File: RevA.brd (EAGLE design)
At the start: 106 x 53 mm, 61 parts, among them IC1 MAX31855, IC10 DS3231/SO, IC3 MAX31855, IC4 MAX31855, IC5 MAX31855, IC9 ATMEGA32U4-AU, J1 1X2-3.5MM, J2 1X2-3.5MM, J3 1X2-3.5MM, J4 1X2-3.5MM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

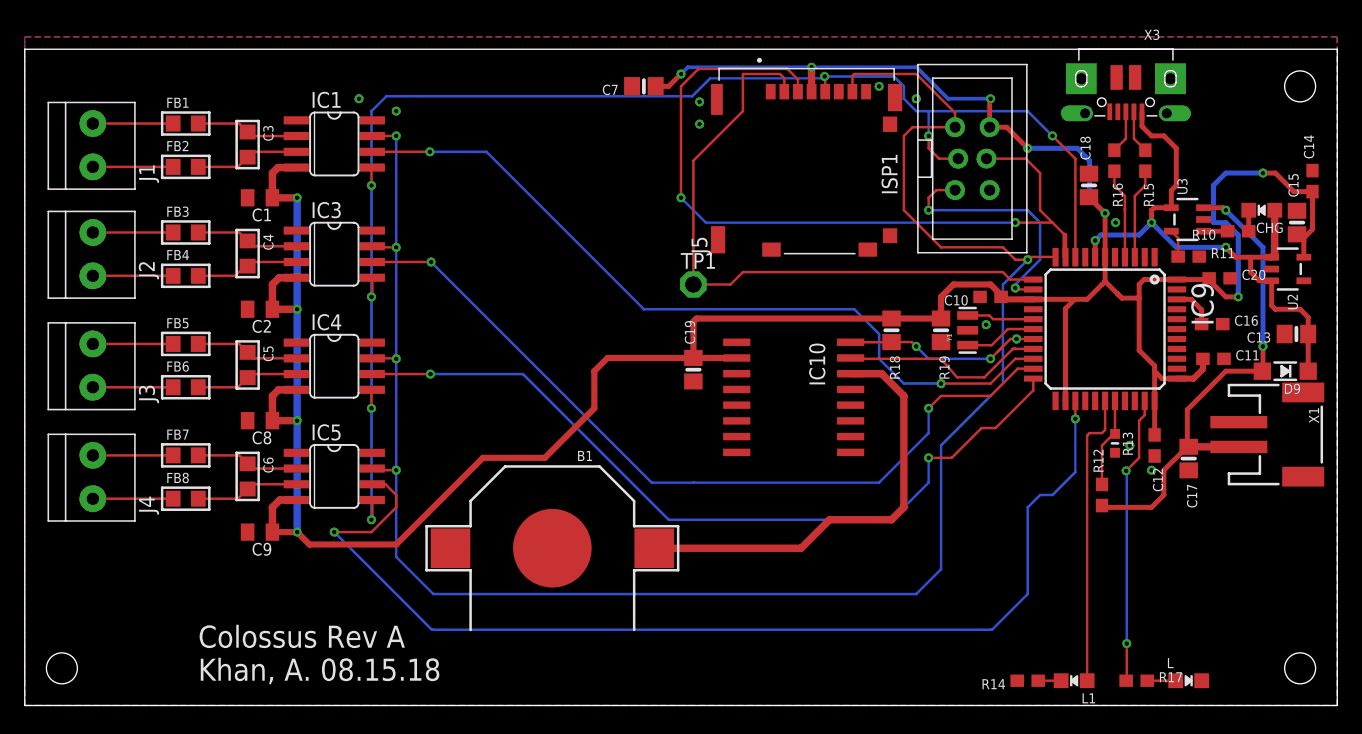
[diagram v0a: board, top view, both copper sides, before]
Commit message: Reduced Footprint
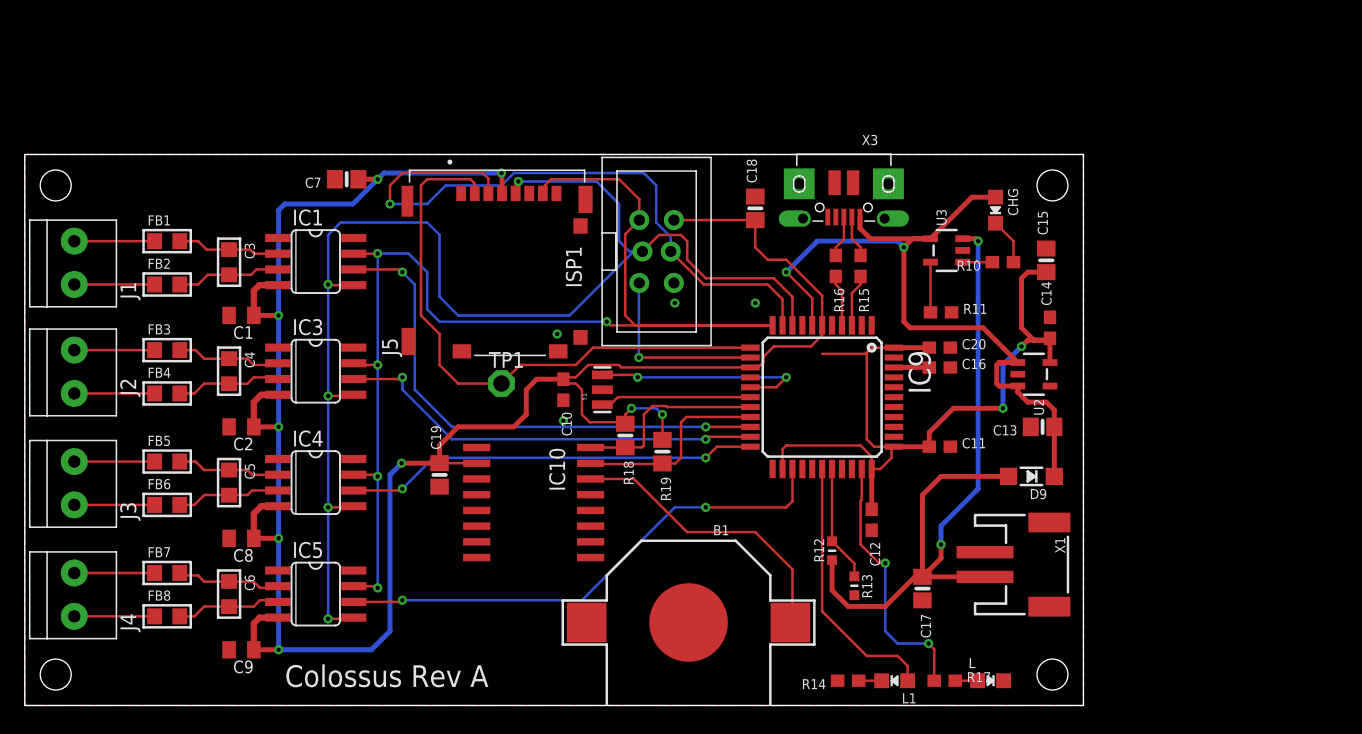
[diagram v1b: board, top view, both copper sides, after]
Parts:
- R12: device microbuilder:0603-NO -> microbuilder:_0603MP
- moved C10 35.3 mm to (43.5, 25.5), turned to 270 degrees
- moved Y1 29.9 mm to (46.6, 25.5)
- moved C18 27.0 mm to (59.0, 40.1)
- moved ISP1 26.6 mm to (51.0, 36.7)
- moved J5 26.3 mm to (38.1, 35.0)
- moved C7 25.1 mm to (26.0, 42.5)
- moved R19 24.5 mm to (51.5, 20.5)
- moved R15 24.5 mm to (67.5, 35.5)
- moved X3 24.3 mm to (66.2, 40.2)
- moved C14 24.3 mm to (82.8, 30.5)
- moved R16 24.1 mm to (65.5, 35.5)
- moved R13 24.0 mm to (67.0, 9.67)
- moved C17 23.9 mm to (72.5, 9.44)
- moved C12 23.6 mm to (68.4, 15.0)
- moved IC9 23.5 mm to (64.4, 24.9)
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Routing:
- net MISO: track 153.0 -> 102.2 mm
- net CS-4: track 87.8 -> 41.4 mm
- net CS-3: track 64.7 -> 33.5 mm
- net CS-2: track 65.7 -> 34.8 mm
- net CS-1: track 63.1 -> 42.3 mm
- net VBAT: track 40.9 -> 60.8 mm
- net VBUS: track 46.5 -> 62.8 mm, vias 3 -> 2
- net N$29: track 6.07 -> 18.7 mm, vias 0 -> 2
- net VCR: track 35.6 -> 23.7 mm
- net MOSI: track 63.7 -> 52.7 mm, vias 2 -> 1
- net SCK: track 115.5 -> 106.8 mm, vias 7 -> 5
- net N$30: track 5.84 -> 12.3 mm
- net +3V3: track 254.7 -> 248.5 mm
- net RST: track 20.4 -> 15.2 mm, vias 2 -> 1
- net SD_CS: track 51.3 -> 47.5 mm
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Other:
- board size 106 x 53 mm -> 85.5 x 44.5 mm
- board text added: "Colossus Rev A"
- board text removed: "Colossus Rev A Khan, A. 08.15.18"

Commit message: Added BOM
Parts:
- added C21: 10µF, microbuilder:0805-NO
- moved C16 2.87 mm to (72.2, 24.9), turned to 270 degrees
- moved D9 1.92 mm to (82.8, 19.7), turned to 270 degrees
- moved R11 1.72 mm to (73.2, 33.2), turned to 270 degrees
- moved C11 1.58 mm to (72.4, 20.4), turned to 270 degrees
- moved C13 1.50 mm to (80.7, 22.5), turned to 90 degrees
- moved C20 0.85 mm to (73.9, 28.1), turned to 270 degrees
- moved R10 0.71 mm to (78.5, 36.3), turned to 270 degrees
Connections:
- net GND: now also C21.1
- net VBUS: now also C21.2
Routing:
- net +3V3: track 248.5 -> 252.1 mm
- net VBUS: track 62.8 -> 66.2 mm
- net VBAT: track 60.8 -> 64.0 mm
- net N$27: track 4.05 -> 1.70 mm
- net N$25: track 3.75 -> 1.84 mm
- net SCK: track 106.8 -> 105.2 mm, vias 5 -> 6

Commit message: Final Traces
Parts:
- moved C11 12.8 mm to (60.0, 17.1), turned to 180 degrees
- moved D9 2.55 mm to (80.3, 19.2)
- moved C13 1.13 mm to (81.5, 23.3), turned to 0 degrees
- moved Y1 0.50 mm to (47.1, 25.5)
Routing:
- net MISO: track 102.2 -> 90.9 mm
- net VBAT: track 64.0 -> 54.7 mm
- net N$29: track 18.7 -> 11.9 mm, vias 2 -> 0
- net VBUS: track 66.2 -> 59.4 mm
- net RST: track 15.2 -> 11.5 mm
- net N$30: track 12.3 -> 11.7 mm
- net GND: track 0.00 -> 0.62 mm, vias 8 -> 28

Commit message: Cleaned up the layout
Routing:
- net GND: vias 28 -> 48
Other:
- board text added: "+"

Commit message: Final cleanup
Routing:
- net GND: vias 48 -> 59
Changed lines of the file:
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@@
 <drawing>
 <settings>
-<setting alwaysvectorfont="yes"/>
+<setting alwaysvectorfont="no"/>
 <setting verticaltext="up"/>
 </settings>
@@
 </layers>
 <board>
-<fusionsync huburn="a.cGVyc29uYWw6dWUyYmRkYjQx" projecturn="a.cGVyc29uYWw6dWUyYmRkYjQxIzIwMTgwNTAyMTMwMjU4MzAx" f3durn="urn:adsk.wipprod:dm.lineage:a68wfmUxQy2LyGLi9FcYGg" pcbguid="62a8e096-691a-4df0-bd8f-1dbb8bf064d3" lastpulledtime="" lastsyncedchangeguid="620a17bd-b7ee-07cf-b851-2800ced5cc59"/>
+<fusionsync huburn="a.cGVyc29uYWw6dWUyYmRkYjQx" projecturn="a.cGVyc29uYWw6dWUyYmRkYjQxIzIwMTgwNTAyMTMwMjU4MzAx" f3durn="urn:adsk.wipprod:dm.lineage:a68wfmUxQy2LyGLi9FcYGg" pcbguid="62a8e096-691a-4df0-bd8f-1dbb8bf064d3" lastpulledtime="" lastsyncedchangeguid="5deacc8e-e9a5-6dbb-9bdc-3b0ce5d54393"/>
 <plain>
 <wire x1="0" y1="0" x2="85.5" y2="0" width="0" layer="20"/>
@@
 <hole x="2.5" y="42" drill="2.5"/>
 <text x="24.5" y="1.5" size="1.778" layer="29" font="vector" ratio="12">Colossus Rev A</text>
-<text x="73.875" y="8.375" size="2" layer="25">+</text>
+<text x="73.875" y="8.25" size="2" layer="25">+</text>
 </plain>
 <attributes>
@@
 <via x="49" y="17.5" extent="1-16" drill="0.35"/>
 <via x="53.25" y="19.25" extent="1-16" drill="0.35"/>
+<via x="44.5" y="28.5" extent="1-16" drill="0.35"/>
+<via x="78.125" y="23" extent="1-16" drill="0.35"/>
+<via x="76.125" y="18" extent="1-16" drill="0.35"/>
+<via x="70.25" y="3.25" extent="1-16" drill="0.35"/>
+<via x="68.75" y="6.25" extent="1-16" drill="0.35"/>
+<via x="30.25" y="24.75" extent="1-16" drill="0.35"/>
+<via x="29.25" y="19.75" extent="1-16" drill="0.35"/>
+<via x="31" y="16.625" extent="1-16" drill="0.35"/>
+<via x="78.5" y="18.25" extent="1-16" drill="0.35"/>
+<via x="63.75" y="38.25" extent="1-16" drill="0.35"/>
+<via x="70.625" y="11.25" extent="1-16" drill="0.35"/>
 </signal>
 <signal name="CS-1">

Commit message: Adding gerber files
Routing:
- net GND: vias 59 -> 71
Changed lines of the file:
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@@
 <layer number="26" name="bNames" color="7" fill="1" visible="no" active="yes"/>
 <layer number="27" name="tValues" color="7" fill="1" visible="yes" active="yes"/>
-<layer number="28" name="bValues" color="7" fill="1" visible="no" active="yes"/>
+<layer number="28" name="bValues" color="7" fill="1" visible="yes" active="yes"/>
 <layer number="29" name="tStop" color="7" fill="3" visible="yes" active="yes"/>
 <layer number="30" name="bStop" color="7" fill="6" visible="yes" active="yes"/>
@@
 </layers>
 <board>
-<fusionsync huburn="a.cGVyc29uYWw6dWUyYmRkYjQx" projecturn="a.cGVyc29uYWw6dWUyYmRkYjQxIzIwMTgwNTAyMTMwMjU4MzAx" f3durn="urn:adsk.wipprod:dm.lineage:a68wfmUxQy2LyGLi9FcYGg" pcbguid="62a8e096-691a-4df0-bd8f-1dbb8bf064d3" lastpulledtime="" lastsyncedchangeguid="5deacc8e-e9a5-6dbb-9bdc-3b0ce5d54393"/>
+<fusionsync huburn="a.cGVyc29uYWw6dWUyYmRkYjQx" projecturn="a.cGVyc29uYWw6dWUyYmRkYjQxIzIwMTgwNTAyMTMwMjU4MzAx" f3durn="urn:adsk.wipprod:dm.lineage:a68wfmUxQy2LyGLi9FcYGg" pcbguid="62a8e096-691a-4df0-bd8f-1dbb8bf064d3" lastpulledtime="" lastsyncedchangeguid="a59ad179-57a4-5a50-164f-14a713c3d576"/>
 <plain>
 <wire x1="0" y1="0" x2="85.5" y2="0" width="0" layer="20"/>
@@
 </element>
 <element name="C10" library="microbuilder" package="0603-NO" value="1uF" x="43.5" y="25.5" smashed="yes" rot="R270">
-<attribute name="NAME" x="42.748" y="22.972" size="0.8128" layer="25" font="vector" ratio="10"/>
+<attribute name="NAME" x="42.248" y="23.097" size="0.8128" layer="25" font="vector" ratio="10"/>
 </element>
 <element name="C11" library="microbuilder" package="0603-NO" value="1uF" x="60.025" y="17.15" smashed="yes" rot="R180">
@@
 <contactref element="C20" pad="2"/>
 <via x="43" y="30" extent="1-16" drill="0.35"/>
-<via x="45.75" y="23.75" extent="1-16" drill="0.35"/>
+<via x="44.5" y="22.875" extent="1-16" drill="0.35"/>
 <via x="52.5" y="32.5" extent="1-16" drill="0.35"/>
 <via x="59" y="32.5" extent="1-16" drill="0.35"/>
@@
 <via x="63.75" y="38.25" extent="1-16" drill="0.35"/>
 <via x="70.625" y="11.25" extent="1-16" drill="0.35"/>
+<via x="33.375" y="32.125" extent="1-16" drill="0.35"/>
+<via x="32.75" y="29.75" extent="1-16" drill="0.35"/>
+<via x="35.25" y="26.75" extent="1-16" drill="0.35"/>
+<via x="40.25" y="26.75" extent="1-16" drill="0.35"/>
+<via x="39.25" y="23.75" extent="1-16" drill="0.35"/>
+<via x="30.75" y="33.75" extent="1-16" drill="0.35"/>
+<via x="67.25" y="3.75" extent="1-16" drill="0.35"/>
+<via x="49.5" y="42.125" extent="1-16" drill="0.35"/>
+<via x="79.375" y="24.875" extent="1-16" drill="0.35"/>
+<via x="73.25" y="14.875" extent="1-16" drill="0.35"/>
+<via x="70" y="36.625" extent="1-16" drill="0.35"/>
+<via x="45.25" y="9.75" extent="1-16" drill="0.35"/>
 </signal>
 <signal name="CS-1">
@@
 <wire x1="46.375" y1="28.375" x2="54.625" y2="28.375" width="0.4" layer="1"/>
 <wire x1="33.5" y1="19.57" x2="33.505" y2="19.565" width="0.2032" layer="1"/>
-<wire x1="33.505" y1="19.565" x2="36.5" y2="19.565" width="0.2032" layer="1"/>
+<wire x1="33.505" y1="19.565" x2="36.5" y2="19.565" width="0.4" layer="1"/>
 <wire x1="68.4" y1="19.1" x2="68.4" y2="16" width="0.4" layer="1"/>
 <wire x1="68.4" y1="16" x2="68.4" y2="15.85" width="0.4" layer="1"/>
@@
 <wire x1="81" y1="35" x2="80.5" y2="34.5" width="0.4" layer="1"/>
 <wire x1="48.5" y1="22.75" x2="48.625" y2="22.875" width="0.2032" layer="1"/>
-<wire x1="45.625" y1="22.875" x2="45" y2="23.5" width="0.2032" layer="1"/>
-<wire x1="45.625" y1="22.875" x2="48.625" y2="22.875" width="0.2032" layer="1"/>
+<wire x1="45.625" y1="22.875" x2="45" y2="23.5" width="0.4" layer="1"/>
+<wire x1="45.625" y1="22.875" x2="48.625" y2="22.875" width="0.4" layer="1"/>
 <wire x1="20.5" y1="4.5" x2="28" y2="4.5" width="0.4" layer="16"/>
 <wire x1="30.43" y1="19.57" x2="33.5" y2="19.57" width="0.4" layer="1"/>
@@
 <wire x1="78.5" y1="27.5" x2="80.5" y2="29.5" width="0.4" layer="16"/>
 <via x="80.5" y="29.5" extent="1-16" drill="0.35"/>
-<wire x1="48.5" y1="22.75" x2="48.5" y2="23.5" width="0.2032" layer="1"/>
-<wire x1="48.5" y1="23.5" x2="49" y2="24" width="0.2032" layer="1"/>
+<wire x1="48.5" y1="22.75" x2="48.5" y2="23.5" width="0.4" layer="1"/>
+<wire x1="48.5" y1="23.5" x2="49" y2="24" width="0.4" layer="1"/>
 <via x="49" y="24" extent="1-16" drill="0.35"/>
-<wire x1="49" y1="24" x2="50.875" y2="24" width="0.2032" layer="16"/>
-<wire x1="50.875" y1="24" x2="51.5" y2="23.375" width="0.2032" layer="16"/>
+<wire x1="49" y1="24" x2="50.875" y2="24" width="0.4" layer="16"/>
+<wire x1="50.875" y1="24" x2="51.5" y2="23.375" width="0.4" layer="16"/>
 <via x="51.5" y="23.375" extent="1-16" drill="0.35"/>
-<wire x1="51.5" y1="23.375" x2="51.5" y2="21.45" width="0.2032" layer="1"/>
+<wire x1="51.5" y1="23.375" x2="51.5" y2="21.45" width="0.4" layer="1"/>
 <via x="30.43" y="19.57" extent="1-16" drill="0.35"/>
 <wire x1="70.2" y1="28.9" x2="73.9" y2="28.9" width="0.4" layer="1"/>
@@
 <wire x1="68.4" y1="19.1" x2="68.5" y2="19.1" width="0.2032" layer="1"/>
 <wire x1="68.5" y1="19.1" x2="68.5" y2="20.9" width="0.4" layer="1"/>
-<wire x1="61.2" y1="19.1" x2="61.2" y2="17.475" width="0.2032" layer="1"/>
+<wire x1="61.2" y1="19.1" x2="61.2" y2="17.475" width="0.4" layer="1"/>
 <wire x1="61.2" y1="17.475" x2="60.875" y2="17.15" width="0.2032" layer="1"/>
 <wire x1="78.5" y1="24" x2="78" y2="24" width="0.4" layer="1"/>
@@
 <wire x1="68.1" y1="20.9" x2="66" y2="23" width="0.4" layer="1"/>
 <wire x1="45" y1="27" x2="46.375" y2="28.375" width="0.4" layer="1"/>
-<wire x1="45" y1="23.5" x2="45" y2="26.5" width="0.2032" layer="1"/>
+<wire x1="45" y1="23.5" x2="45" y2="26.5" width="0.4" layer="1"/>
 <wire x1="45" y1="26.5" x2="45" y2="27" width="0.4" layer="1"/>
 <wire x1="43.5" y1="26.35" x2="43.65" y2="26.5" width="0.2032" layer="1"/>
